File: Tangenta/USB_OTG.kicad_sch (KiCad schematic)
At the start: 1 part, among them J11 TYPEC-304-ACP16

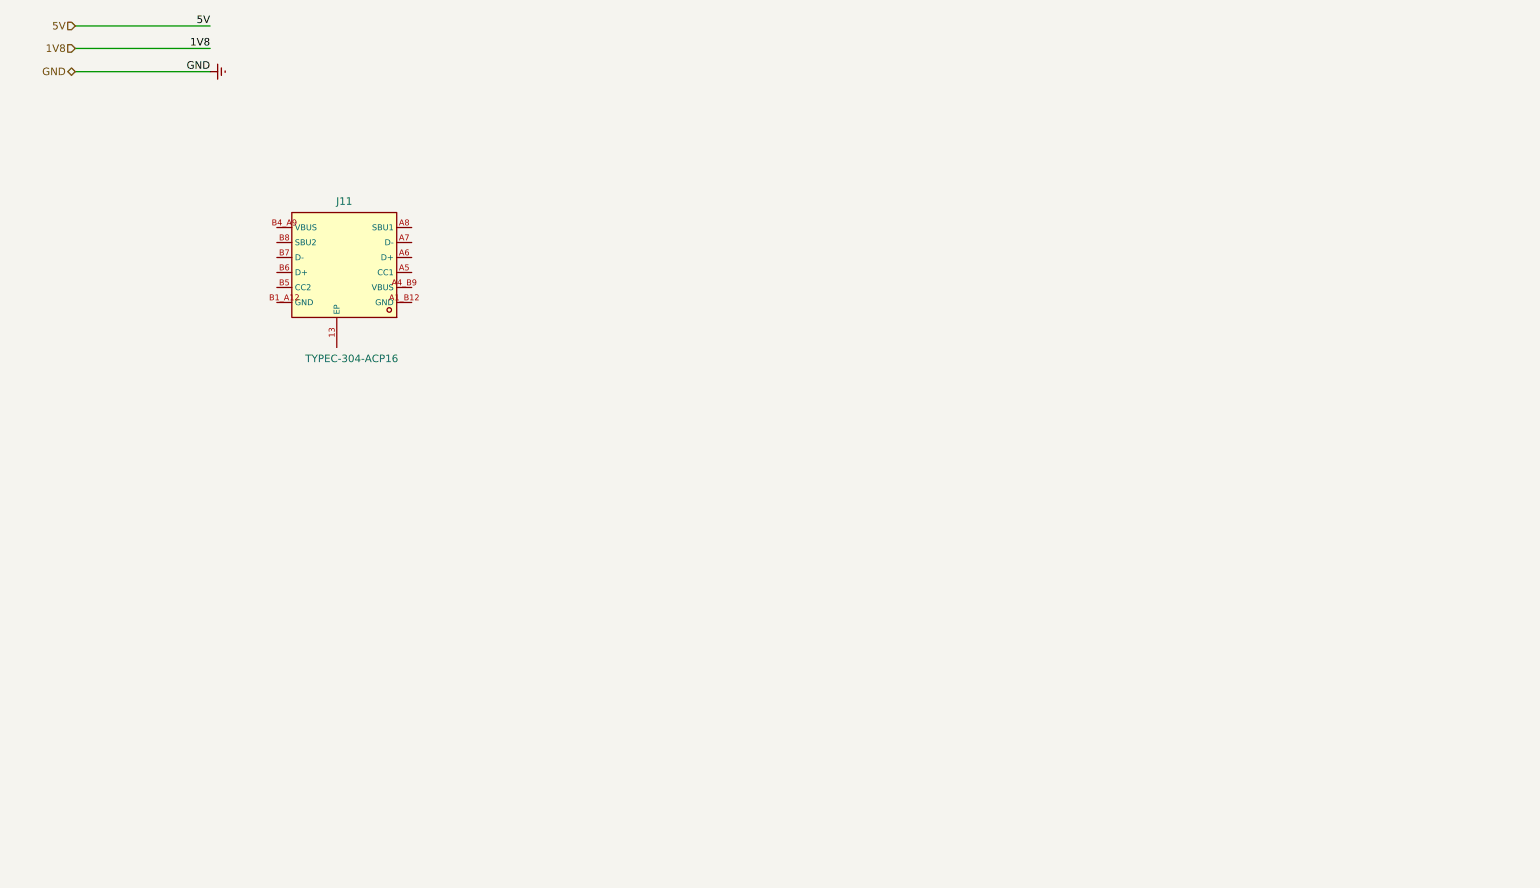
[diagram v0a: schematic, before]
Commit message: Adding Zener 5.8V.
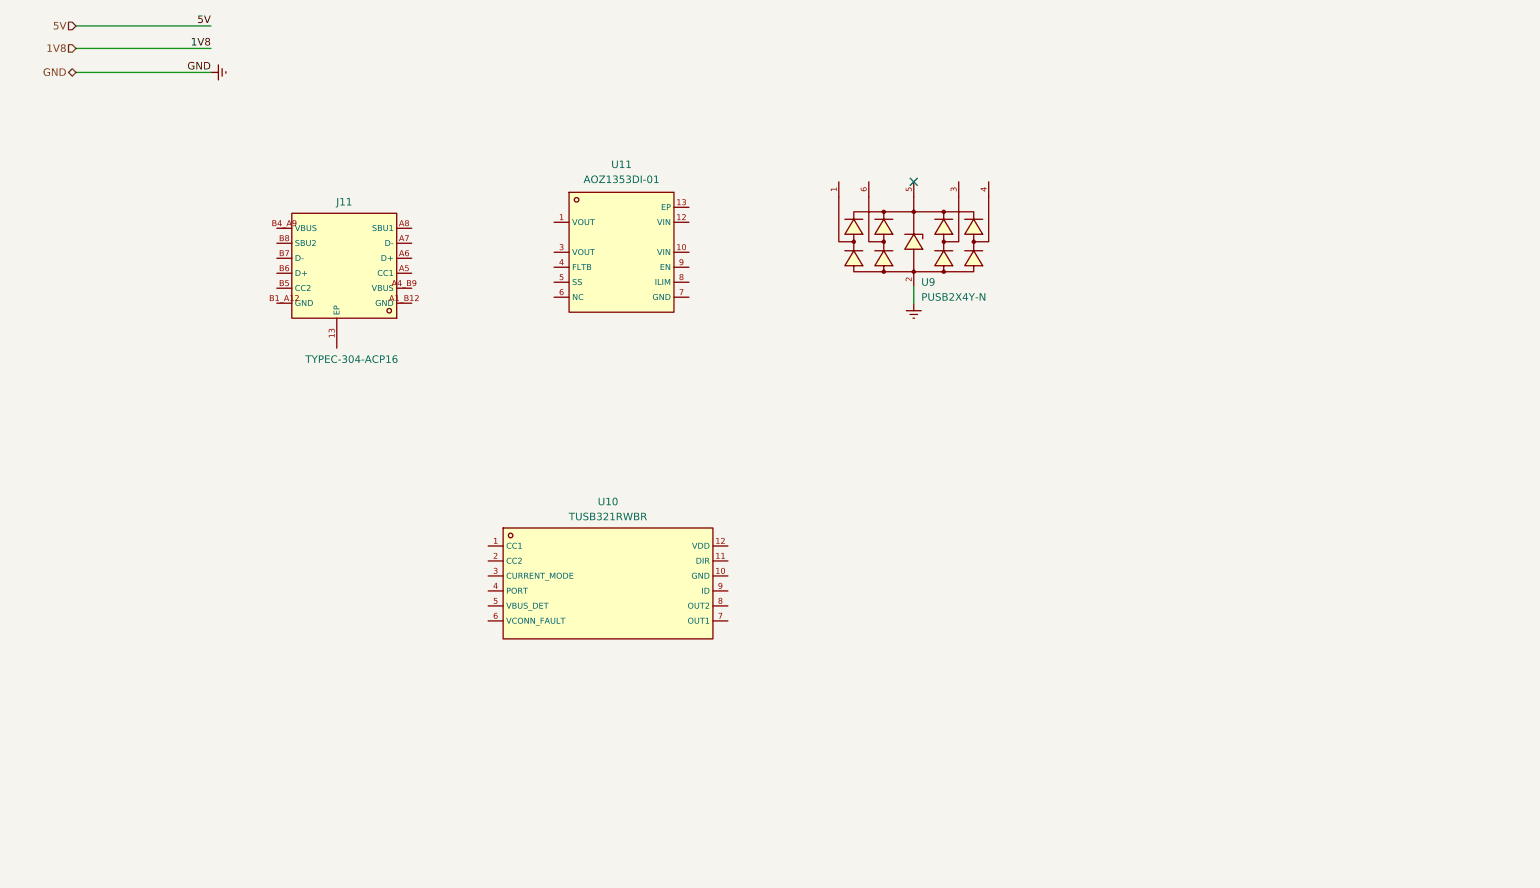
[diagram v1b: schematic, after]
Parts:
- added U10: TUSB321RWBR, TUSB321RWBR:TUSB321RWBR, symbol TUSB321RWBR:TUSB321RWBR
- added U11: AOZ1353DI-01, AOZ1353DI01:AOZ1353DI01, symbol AOZ1353DI01:AOZ1353DI-01
- added U9: PUSB2X4Y-N, USB_ESD:USB_ESD, symbol USB_ESD:PUSB2X4Y-N
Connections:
- net GNDREF: now also U9.2 (GND)
- no-connect marks 0 -> 1
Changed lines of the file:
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@@
 (kicad_sch (version 20230121) (generator eeschema)
   (paper "A4")
-  (wire (pts (xy 58.547 27.559) (xy 35.687 27.559))
-    (stroke (width 0) (type default))
-  )
-  (wire (pts (xy 58.547 23.622) (xy 35.687 23.622))
-    (stroke (width 0) (type default))
-  )
-  (wire (pts (xy 58.547 19.812) (xy 35.687 19.812))
-    (stroke (width 0) (type default))
-  )
-  (label "GND" (at 58.547 27.559 180) (fields_autoplaced)
+  (no_connect (at 177.8 46.228))
+  (wire (pts (xy 177.8 64.008) (xy 177.8 66.802))
+    (stroke (width 0) (type default))
+  )
+  (wire (pts (xy 58.674 27.686) (xy 35.814 27.686))
+    (stroke (width 0) (type default))
+  )
+  (wire (pts (xy 58.674 23.622) (xy 35.814 23.622))
+    (stroke (width 0) (type default))
+  )
+  (wire (pts (xy 58.674 19.812) (xy 35.814 19.812))
+    (stroke (width 0) (type default))
+  )
+  (label "GND" (at 58.674 27.686 180) (fields_autoplaced)
     (effects (font (size 1.27 1.27)) (justify right bottom))
   )
-  (label "5V" (at 58.547 19.812 180) (fields_autoplaced)
+  (label "5V" (at 58.674 19.812 180) (fields_autoplaced)
     (effects (font (size 1.27 1.27)) (justify right bottom))
   )
-  (label "1V8" (at 58.547 23.622 180) (fields_autoplaced)
+  (label "1V8" (at 58.674 23.622 180) (fields_autoplaced)
     (effects (font (size 1.27 1.27)) (justify right bottom))
   )
-  (hierarchical_label "GND" (shape bidirectional) (at 35.687 27.559 180) (fields_autoplaced)
+  (hierarchical_label "GND" (shape bidirectional) (at 35.814 27.686 180) (fields_autoplaced)
     (effects (font (size 1.27 1.27)) (justify right))
   )
-  (hierarchical_label "1V8" (shape input) (at 35.687 23.622 180) (fields_autoplaced)
+  (hierarchical_label "1V8" (shape input) (at 35.814 23.622 180) (fields_autoplaced)
     (effects (font (size 1.27 1.27)) (justify right))
   )
-  (hierarchical_label "5V" (shape input) (at 35.687 19.812 180) (fields_autoplaced)
+  (hierarchical_label "5V" (shape input) (at 35.814 19.812 180) (fields_autoplaced)
     (effects (font (size 1.27 1.27)) (justify right))
   )
-  (symbol (lib_id "USB_TYPEC:TYPEC-304-ACP16") (at 82.55 61.595 180) (unit 1)
+  (symbol (lib_id "USB_TYPEC:TYPEC-304-ACP16") (at 82.55 61.722 180) (unit 1)
     (in_bom yes) (on_board yes) (dnp no)
-    (property "Reference" "J11" (at 81.28 49.53 0)
-      (effects (font (size 1.27 1.27)))
-    )
-    (property "Value" "TYPEC-304-ACP16" (at 82.55 76.2 0)
-      (effects (font (size 1.27 1.27)))
-    )
-    (property "Footprint" "USB_TYPEC:USB_TYPEC" (at 80.01 47.625 0)
-      (effects (font (size 1.27 1.27) italic) hide)
-    )
-    (property "Datasheet" "https://img.jlc.com/pdf/applyPasteComponent/2022-02-23/91586W/67ceeeb81a9f4c1f8ea00a3628213c3d/USBC16P.pdf" (at 91.44 42.545 0)
-      (effects (font (size 1.27 1.27)) (justify left) hide)
-    )
-    (property "LCSC" "C2982555" (at 80.01 45.085 0)
+    (property "Reference" "J11" (at 81.28 49.657 0)
+      (effects (font (size 1.27 1.27)))
+    )
+    (property "Value" "TYPEC-304-ACP16" (at 82.55 76.327 0)
+      (effects (font (size 1.27 1.27)))
+    )
+    (property "Footprint" "USB_TYPEC:USB_TYPEC" (at 80.01 47.752 0)
+      (effects (font (size 1.27 1.27) italic) hide)
+    )
+    (property "Datasheet" "https://img.jlc.com/pdf/applyPasteComponent/2022-02-23/91586W/67ceeeb81a9f4c1f8ea00a3628213c3d/USBC16P.pdf" (at 91.44 42.672 0)
+      (effects (font (size 1.27 1.27)) (justify left) hide)
+    )
+    (property "LCSC" "C2982555" (at 80.01 45.212 0)
       (effects (font (size 1.27 1.27)) hide)
     )
@@
     )
   )
-  (symbol (lib_id "power:GNDREF") (at 58.547 27.559 90) (unit 1)
-    (in_bom yes) (on_board yes) (dnp no) (fields_autoplaced)
-    (property "Reference" "#PWR013" (at 64.897 27.559 0)
-      (effects (font (size 1.27 1.27)) hide)
-    )
-    (property "Value" "GNDREF" (at 62.357 27.559 90)
+  (symbol (lib_id "power:GNDREF") (at 58.674 27.686 90) (unit 1)
+    (in_bom yes) (on_board yes) (dnp no) (fields_autoplaced)
+    (property "Reference" "#PWR013" (at 65.024 27.686 0)
+      (effects (font (size 1.27 1.27)) hide)
+    )
+    (property "Value" "GNDREF" (at 62.484 27.686 90)
       (effects (font (size 1.27 1.27)) (justify right) hide)
     )
-    (property "Footprint" "" (at 58.547 27.559 0)
-      (effects (font (size 1.27 1.27)) hide)
-    )
-    (property "Datasheet" "" (at 58.547 27.559 0)
+    (property "Footprint" "" (at 58.674 27.686 0)
+      (effects (font (size 1.27 1.27)) hide)
+    )
+    (property "Datasheet" "" (at 58.674 27.686 0)
       (effects (font (size 1.27 1.27)) hide)
     )
@@
         )
       )
+    )
+  )
+  (symbol (lib_id "power:GNDREF") (at 177.8 66.802 0) (unit 1)
+    (in_bom yes) (on_board yes) (dnp no) (fields_autoplaced)
+    (property "Reference" "#PWR013" (at 177.8 73.152 0)
+      (effects (font (size 1.27 1.27)) hide)
+    )
+    (property "Value" "GNDREF" (at 177.8 70.612 90)
+      (effects (font (size 1.27 1.27)) (justify right) hide)
+    )
+    (property "Footprint" "" (at 177.8 66.802 0)
+      (effects (font (size 1.27 1.27)) hide)
+    )
+    (property "Datasheet" "" (at 177.8 66.802 0)
+      (effects (font (size 1.27 1.27)) hide)
+    )
+    (pin "1")
+    (instances
+      (project "Tangenta"
+        (path "/358d1bcf-7599-4352-8c4d-baa18a5f09e6/d6c05402-162e-441f-bed8-be7996260fb4"
+          (reference "#PWR013") (unit 1)
+        )
+        (path "/358d1bcf-7599-4352-8c4d-baa18a5f09e6/e56d8c10-557c-47b7-a4d3-5b3b43580080"
+          (reference "#PWR037") (unit 1)
+        )
+      )
+    )
+  )
+  (symbol (lib_id "AOZ1353DI01:AOZ1353DI-01") (at 128.27 58.166 0) (unit 1)
+    (in_bom yes) (on_board yes) (dnp no) (fields_autoplaced)
+    (property "Reference" "U11" (at 128.27 43.307 0)
+      (effects (font (size 1.27 1.27)))
+    )
+    (property "Value" "AOZ1353DI-01" (at 128.27 45.847 0)
+      (effects (font (size 1.27 1.27)))
+    )
+    (property "Footprint" "AOZ1353DI01:AOZ1353DI01" (at 132.08 78.105 0)
+      (effects (font (size 1.27 1.27) italic) hide)
+    )
+    (property "Datasheet" "https://atta.szlcsc.com/upload/public/pdf/source/20210424/E490F122344F63F6C3EB83CD3BAB7344.pdf" (at 119.126 75.438 0)
+      (effects (font (size 1.27 1.27)) (justify left) hide)
+    )
+    (property "LCSC" "C2149839" (at 123.952 73.152 0)
+      (effects (font (size 1.27 1.27)) hide)
+    )
+    (pin "1")
+    (pin "10")
+    (pin "12")
+    (pin "13")
+    (pin "3")
+    (pin "4")
+    (pin "5")
+    (pin "6")
+    (pin "7")
+    (pin "8")
+    (pin "9")
+    (instances
+      (project "Tangenta"
+        (path "/358d1bcf-7599-4352-8c4d-baa18a5f09e6/e56d8c10-557c-47b7-a4d3-5b3b43580080"
+          (reference "U11") (unit 1)
+        )
+      )
+    )
+  )
+  (symbol (lib_id "TUSB321RWBR:TUSB321RWBR") (at 125.984 114.3 0) (unit 1)
+    (in_bom yes) (on_board yes) (dnp no) (fields_autoplaced)
+    (property "Reference" "U10" (at 125.984 100.457 0)
+      (effects (font (size 1.27 1.27)))
+    )
+    (property "Value" "TUSB321RWBR" (at 125.984 102.997 0)
+      (effects (font (size 1.27 1.27)))
+    )
+    (property "Footprint" "TUSB321RWBR:TUSB321RWBR" (at 122.174 133.223 0)
+      (effects (font (size 1.27 1.27) italic) hide)
+    )
+    (property "Datasheet" "https://atta.szlcsc.com/upload/public/pdf/source/20210802/C895396_3044DB7B453642D2E172318E9AFDD458.pdf" (at 108.204 130.556 0)
+      (effects (font (size 1.27 1.27)) (justify left) hide)
+    )
+    (property "LCSC" "C139392" (at 112.522 128.27 0)
+      (effects (font (size 1.27 1.27)) hide)
+    )
+    (pin "1")
+    (pin "10")
+    (pin "11")
+    (pin "12")
+    (pin "2")
+    (pin "3")
+    (pin "4")
+    (pin "5")
+    (pin "6")
+    (pin "7")
+    (pin "8")
+    (pin "9")
+    (instances
+      (project "Tangenta"
+        (path "/358d1bcf-7599-4352-8c4d-baa18a5f09e6/e56d8c10-557c-47b7-a4d3-5b3b43580080"
+          (reference "U10") (unit 1)
+        )
+      )
+    )
+  )
+  (symbol (lib_id "USB_ESD:PUSB2X4Y-N") (at 177.8 53.848 0) (unit 1)
+    (in_bom yes) (on_board yes) (dnp no)
+    (property "Reference" "U9" (at 179.07 63.246 0)
+      (effects (font (size 1.27 1.27)) (justify left))
+    )
+    (property "Value" "PUSB2X4Y-N" (at 179.07 65.786 0)
+      (effects (font (size 1.27 1.27)) (justify left))
+    )
+    (property "Footprint" "USB_ESD:USB_ESD" (at 173.736 75.311 0)
+      (effects (font (size 1.27 1.27) italic) hide)
+    )
+    (property "Datasheet" "https://atta.szlcsc.com/upload/public/pdf/source/20201222/C968097_8CE85012EDEDFE3141661B63FCE24852.pdf" (at 165.227 77.47 0)
+      (effects (font (size 1.27 1.27)) (justify left) hide)
+    )
+    (property "LCSC" "C920302" (at 169.291 73.025 0)
+      (effects (font (size 1.27 1.27)) hide)
+    )
+    (pin "1")
+    (pin "2")
+    (pin "3")
+    (pin "4")
+    (pin "5")
+    (pin "6")
+    (instances
+      (project "Tangenta"
+        (path "/358d1bcf-7599-4352-8c4d-baa18a5f09e6/e56d8c10-557c-47b7-a4d3-5b3b43580080"
+          (reference "U9") (unit 1)
+        )
+      )

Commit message: USB DualRole in progress...
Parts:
- added C1 (x2): 100uF, Capacitor_SMD:C_0402_1005Metric, symbol Device:C_Small
- added C1: 1nF, Capacitor_SMD:C_0402_1005Metric, symbol Device:C_Small
- added C1: 10nF, Capacitor_SMD:C_0402_1005Metric, symbol Device:C_Small
- added C1: 100nF, Capacitor_SMD:C_0402_1005Metric, symbol Device:C_Small
- added C1: 4.7uF, Capacitor_SMD:C_0402_1005Metric, symbol Device:C_Small
- added D5: BZT52C6V2S-7-F, BZT52C6V2S-7-F:BZT52C6V2S-7-F, symbol BZT52C6V2S-7-F:BZT52C6V2S-7-F
- added R2 (x2): 100k, Resistor_SMD:R_0402_1005Metric, symbol Device:R_Small_US
- added R2: 10k, Resistor_SMD:R_0402_1005Metric, symbol Device:R_Small_US
- added R2: 28.7k, Resistor_SMD:R_0402_1005Metric, symbol Device:R_Small_US
- added U12: PUSB2X4Y-N, USB_ESD:USB_ESD, symbol USB_ESD:PUSB2X4Y-N
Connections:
- net 1V8: now also R2.1
- net 5V: now also U11.10 (VIN), U11.12 (VIN), C1.2, C1.2, C1.2
- net GNDREF: now also U11.13 (EP), U11.7 (GND), C1.1, C1.1, C1.1, C1.1, R2.1, R2.1, U12.2 (GND)
- net USB_DR.VBUS: now reaches U11.1 (VOUT)
- net USB_DR.VBUS: now also U11.3 (VOUT), C1.2, C1.2, D5.1 (K), R2.2, U12.1, U12.3, U12.4, U12.6
- net USB_DR.nOC: now reaches U11.4 (FLTB)
- net USB_DR.nOC: now also R2.2
- net at U11.5 (SS): now also C1.2
- net at U11.8 (ILIM): now also R2.2
- net USB_DR.EN: now reaches U11.9 (EN)
- net USB_DR.EN: now also R2.2
- new net: C1.1, C1.1, D5.2 (A), R2.1
- no-connect marks 1 -> 2
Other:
- moved on the sheet: J11, U10, U11, U9

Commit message: Current progress...
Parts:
- added C1: 100nF, Capacitor_SMD:C_0402_1005Metric, symbol Device:C_Small
- added C1: 100uF, Capacitor_SMD:C_0402_1005Metric, symbol Device:C_Small
- added R2: 887k, Resistor_SMD:R_0402_1005Metric, symbol Device:R_Small_US
- added R2: 100k, Resistor_SMD:R_0402_1005Metric, symbol Device:R_Small_US
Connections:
- net 1V8: now also R2.2
- net 5V: now also U10.12 (VDD), C1.2, C1.2
- net GNDREF: now also J11.A1_B12 (GND), J11.B1_A12 (GND), U10.10 (GND), C1.1, C1.1
- net USB_DR.ID: now also U10.9 (ID), R2.1
- net USB_DR.N: now also J11.A7 (D-), J11.B7 (D-), U9.3
- net USB_DR.P: now also J11.A6 (D+), J11.B6 (D+), U9.4
- net USB_DR.VBUS: now also J11.A4_B9 (VBUS), J11.B4_A9 (VBUS), R2.1
- net USB_DR_CC1: now reaches J11.A5 (CC1)
- net USB_DR_CC1: now also U10.1 (CC1), U9.6
- net USB_DR_CC2: now reaches J11.B5 (CC2)
- net USB_DR_CC2: now also U10.2 (CC2), U9.1
- net at U10.5 (VBUS_DET): now also R2.2
- no-connect marks 2 -> 10
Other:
- moved on the sheet: J11, U10, U9

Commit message: USB DR schematic done.
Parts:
- added C48: 16CE47FSS, CAP_L5:CAP_L5, symbol CAP_L5:16CE47FSS
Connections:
- net USB_DR.VBUS: now also C48.1
- net CHASSIS: now reaches J11.13 (EP)
- net at C1.1, C1.1, D5.2 (A)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: now also C48.2
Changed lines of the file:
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@@
   (junction (at 229.87 31.242) (diameter 0) (color 0 0 0 0)
   )
+  (junction (at 259.08 43.942) (diameter 0) (color 0 0 0 0)
+  )
   (junction (at 67.818 93.726) (diameter 0) (color 0 0 0 0)
   )
@@
   )
   (junction (at 249.428 31.242) (diameter 0) (color 0 0 0 0)
+  )
+  (junction (at 267.716 31.242) (diameter 0) (color 0 0 0 0)
   )
   (junction (at 254 50.8) (diameter 0) (color 0 0 0 0)
@@
     (stroke (width 0) (type default))
   )
+  (wire (pts (xy 36.068 37.465) (xy 46.863 37.465))
+    (stroke (width 0) (type default))
+  )
   (wire (pts (xy 173.736 38.862) (xy 160.02 38.862))
     (stroke (width 0) (type default))
@@
     (stroke (width 0) (type default))
   )
+  (wire (pts (xy 114.808 160.274) (xy 114.808 161.163))
+    (stroke (width 0) (type default))
+  )
   (wire (pts (xy 229.87 43.942) (xy 229.87 39.116))
     (stroke (width 0) (type default))
@@
     (stroke (width 0) (type default))
   )
+  (wire (pts (xy 267.716 31.242) (xy 267.716 34.036))
+    (stroke (width 0) (type default))
+  )
   (wire (pts (xy 136.398 31.242) (xy 170.434 31.242))
     (stroke (width 0) (type default))
@@
     (stroke (width 0) (type default))
   )
+  (wire (pts (xy 114.808 161.163) (xy 123.698 161.163))
+    (stroke (width 0) (type default))
+  )
   (wire (pts (xy 239.776 39.116) (xy 239.776 43.942))
     (stroke (width 0) (type default))
@@
     (stroke (width 0) (type default))
   )
+  (wire (pts (xy 267.716 43.942) (xy 259.08 43.942))
+    (stroke (width 0) (type default))
+  )
   (wire (pts (xy 202.946 41.402) (xy 202.946 43.18))
     (stroke (width 0) (type default))
@@
     (stroke (width 0) (type default))
   )
+  (wire (pts (xy 267.716 39.116) (xy 267.716 43.942))
+    (stroke (width 0) (type default))
+  )
   (wire (pts (xy 124.968 139.954) (xy 140.716 139.954))
     (stroke (width 0) (type default))
@@
     (stroke (width 0) (type default))
   )
-  (wire (pts (xy 259.08 31.242) (xy 267.462 31.242))
+  (wire (pts (xy 259.08 31.242) (xy 267.716 31.242))
     (stroke (width 0) (type default))
   )
@@
     (stroke (width 0) (type default))
   )
+  (wire (pts (xy 267.716 31.242) (xy 279.4 31.242))
+    (stroke (width 0) (type default))
+  )
   (bus (pts (xy 66.548 39.878) (xy 66.548 45.212))
     (stroke (width 0) (type default))
@@
     (effects (font (size 1.27 1.27)) (justify left bottom))
   )
+  (label "CHASSIS" (at 123.698 161.163 180) (fields_autoplaced)
+    (effects (font (size 1.27 1.27)) (justify right bottom))
+  )
   (label "USB_DR.VBUS" (at 140.716 139.954 180) (fields_autoplaced)
     (effects (font (size 1.27 1.27)) (justify right bottom))
@@
     (effects (font (size 1.27 1.27)) (justify right bottom))
   )
-  (label "USB_DR.VBUS" (at 267.462 31.242 180) (fields_autoplaced)
+  (label "USB_DR.VBUS" (at 279.4 31.242 180) (fields_autoplaced)
+    (effects (font (size 1.27 1.27)) (justify right bottom))
+  )
+  (label "CHASSIS" (at 46.863 37.465 180) (fields_autoplaced)
     (effects (font (size 1.27 1.27)) (justify right bottom))
   )
@@
   )
   (hierarchical_label "1V8" (shape input) (at 36.068 29.464 180) (fields_autoplaced)
+    (effects (font (size 1.27 1.27)) (justify right))
+  )
+  (hierarchical_label "CHASSIS" (shape bidirectional) (at 36.068 37.465 180) (fields_autoplaced)
     (effects (font (size 1.27 1.27)) (justify right))
   )
@@
         )
       )
+    )
+  )
+  (symbol (lib_id "CAP_L5:16CE47FSS") (at 267.716 36.576 0) (unit 1)
+    (in_bom yes) (on_board yes) (dnp no)
+    (property "Reference" "C48" (at 267.97 34.925 0)
+      (effects (font (size 1.27 1.27)) (justify left))
+    )
+    (property "Value" "16CE47FSS" (at 270.129 37.4142 0)
+      (effects (font (size 1.27 1.27)) (justify left) hide)
+    )
+    (property "Footprint" "CAP_L5:CAP_L5" (at 266.446 54.356 0)
+      (effects (font (size 1.27 1.27) italic) hide)
+    )
+    (property "Datasheet" "https://item.szlcsc.com/245725.html" (at 259.334 52.07 0)
+      (effects (font (size 1.27 1.27)) (justify left) hide)
+    )
+    (property "LCSC" "C242026" (at 263.652 49.784 0)
+      (effects (font (size 1.27 1.27)) hide)
+    )
+    (property "Capacitance" "47uF" (at 272.288 36.83 0)
+      (effects (font (size 1.27 1.27)) hide)
+    )
+    (pin "1")
+    (pin "2")
+    (instances
+      (project "Tangenta"
+        (path "/358d1bcf-7599-4352-8c4d-baa18a5f09e6/b1871a4d-6a35-44e2-a9a2-9a4af684371d"
+          (reference "C48") (unit 1)
+        )
+        (path "/358d1bcf-7599-4352-8c4d-baa18a5f09e6/e56d8c10-557c-47b7-a4d3-5b3b43580080"
+          (reference "C58") (unit 1)
+        )
+      )
